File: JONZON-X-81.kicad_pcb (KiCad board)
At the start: 2 copper layers, 63.5 x 101 mm, 30 parts, among them SW1 SW_DIP_x03, U1 AY-3-8910, U2 74HCT74, U3 74HCT08, U4 74HCT11, U5 74HCT02

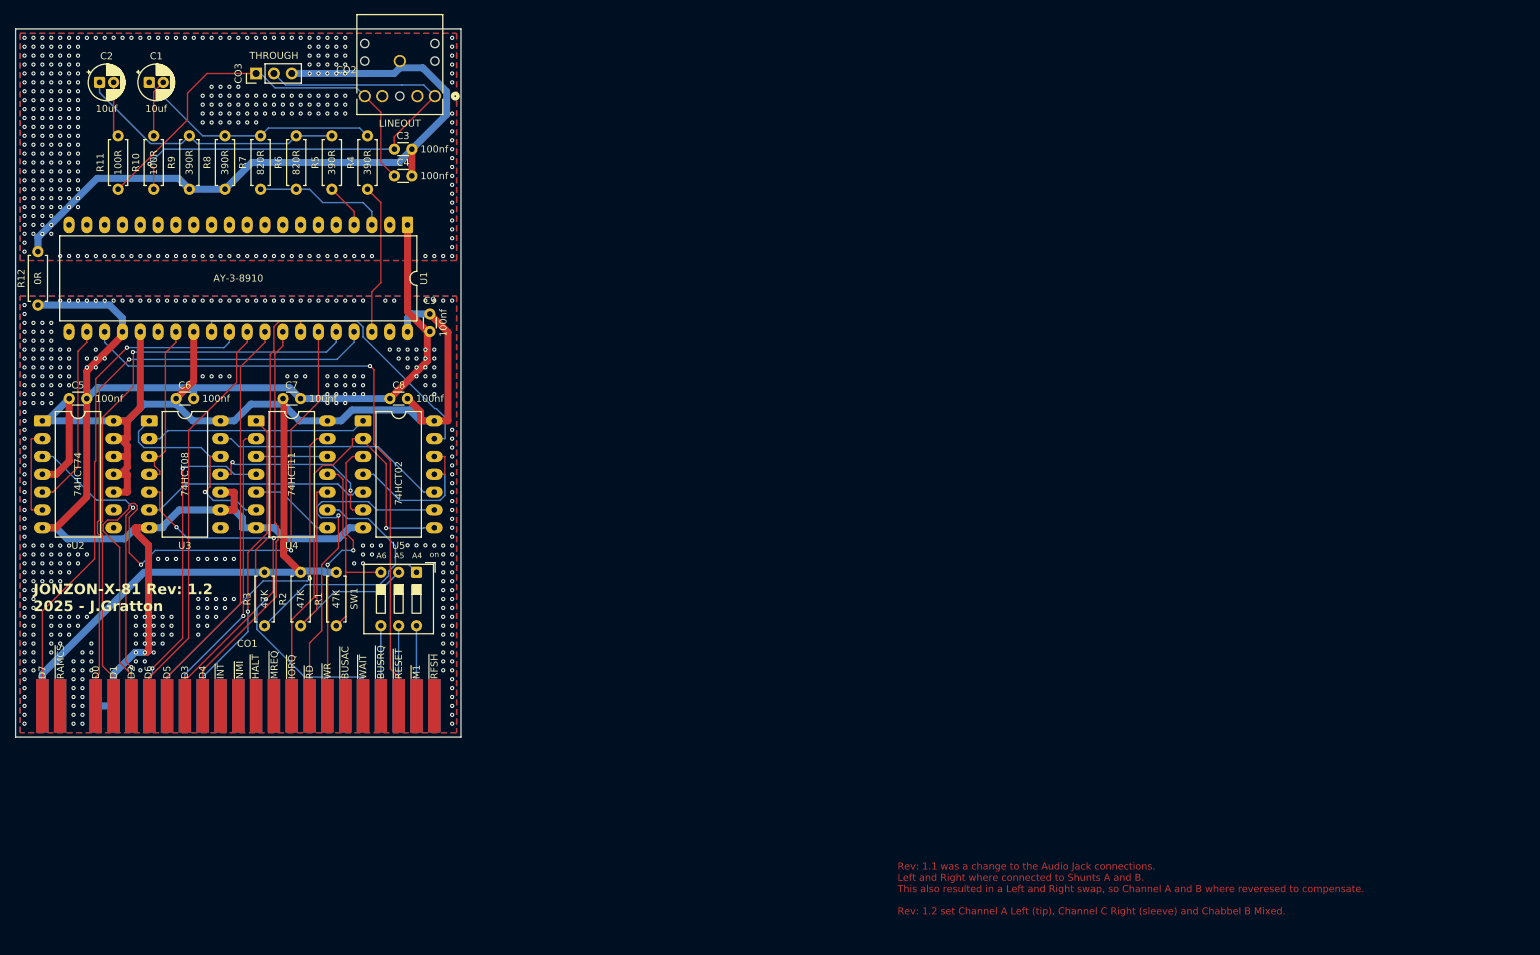
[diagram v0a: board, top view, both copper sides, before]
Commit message: added rev 1.3 to revision history.
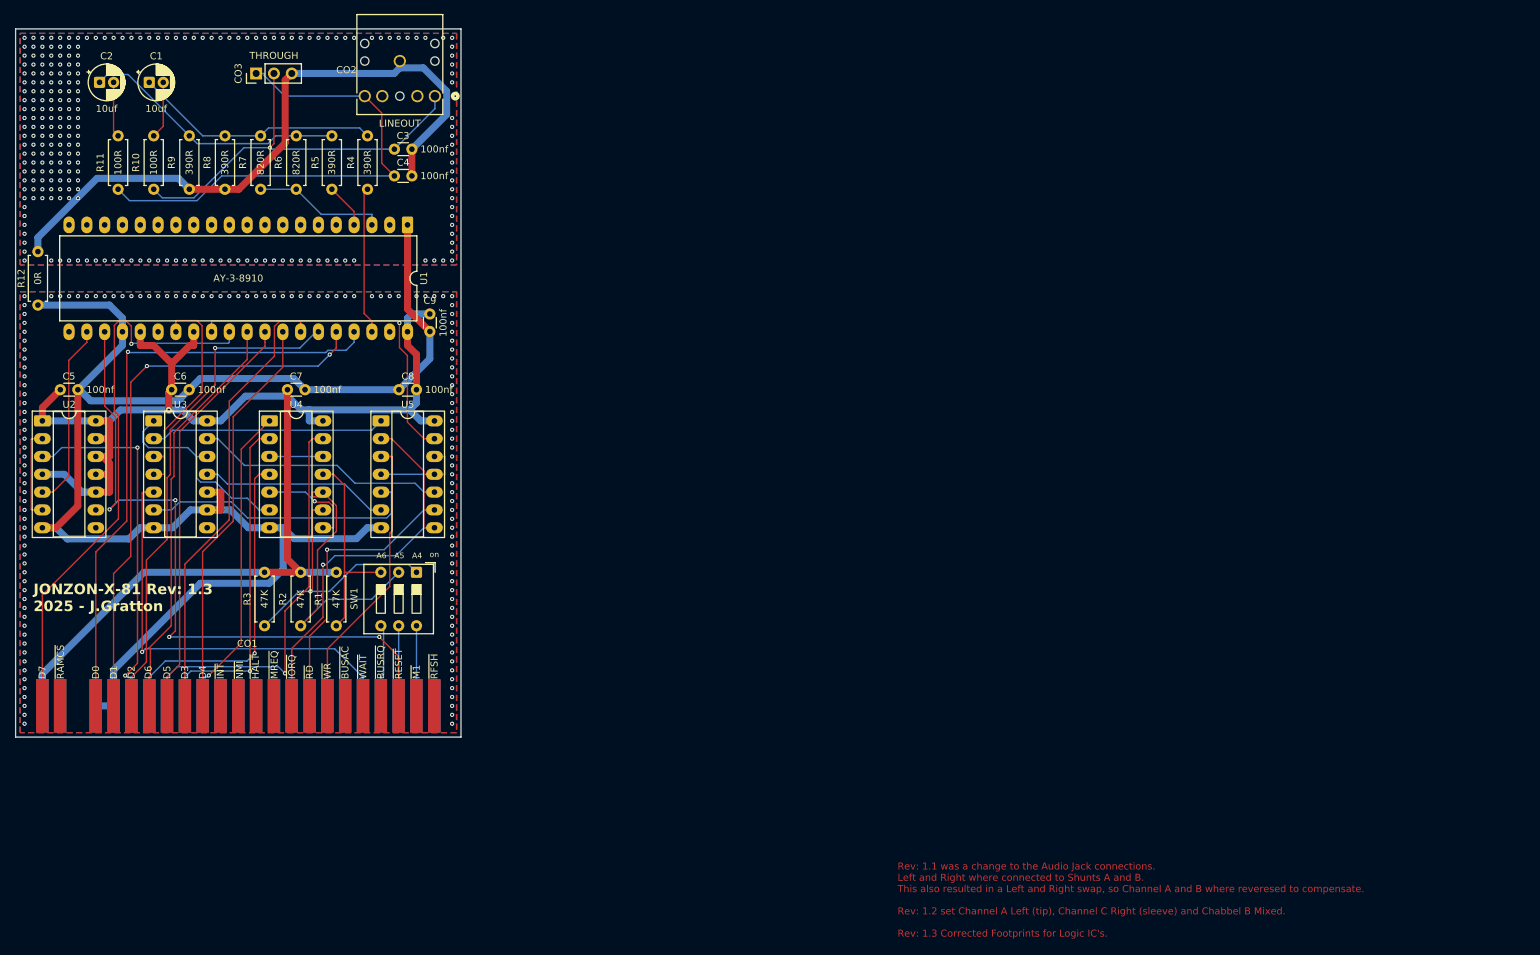
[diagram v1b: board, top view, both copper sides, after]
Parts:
- U2, U3, U4, U5: footprint Package_DIP:DIP-14_W10.16mm_LongPads -> Package_DIP:DIP-14_W7.62mm_Socket_LongPads
- moved U5 2.56 mm to (104.2, 104.1)
- moved U4 1.91 mm to (88.3, 104.1)
- moved C8 1.81 mm to (109.2, 99.7)
- moved C5 1.80 mm to (58.4, 99.7)
- moved C6 1.42 mm to (74.3, 99.7)
- moved C7 1.42 mm to (90.8, 99.7)
- moved U3 0.63 mm to (71.8, 104.1)
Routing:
- net /D2: track 98.6 -> 71.7 mm, vias 2 -> 1
- net VCC: track 235.8 -> 216.2 mm, vias 0 -> 1
- net Net-(CO3-Pin_2): track 73.9 -> 58.6 mm
- net Net-(CO3-Pin_1): track 58.7 -> 71.6 mm
- net GND: track 216.3 -> 226.7 mm, vias 362 -> 141
- net Net-(U5-Pad11): track 23.6 -> 13.2 mm
- net /~{RD}: track 50.8 -> 41.1 mm
- net /BDIR: track 24.6 -> 33.5 mm
- net /D7: track 72.5 -> 80.3 mm
- net /~{IOREQ}: track 65.2 -> 57.7 mm
- net /CLK: track 45.0 -> 52.4 mm
- net GND_AUDIO: track 100.7 -> 93.3 mm, vias 328 -> 240
- net Net-(U3-Pad6): track 32.8 -> 40.1 mm
- net /A1: track 52.1 -> 58.5 mm
- net /~{RESET}: track 91.0 -> 97.0 mm, vias 1 -> 4
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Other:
- board text added: "JONZON-X-81 Rev: 1.3 2025 - J.Gratton"
- board text added: "Rev: 1.3 Corrected Footprints for Logic IC's."
- board text removed: "JONZON-X-81 Rev: 1.2 2025 - J.Gratton"
